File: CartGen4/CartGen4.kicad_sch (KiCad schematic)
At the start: 0 parts

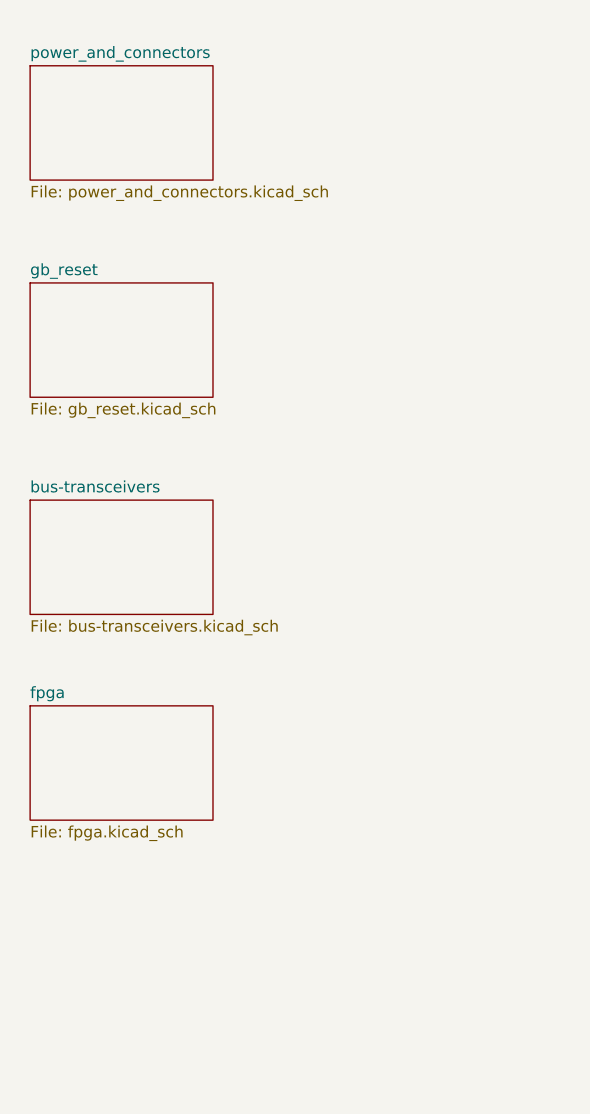
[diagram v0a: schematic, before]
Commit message: Added FPGA and RAM symbols
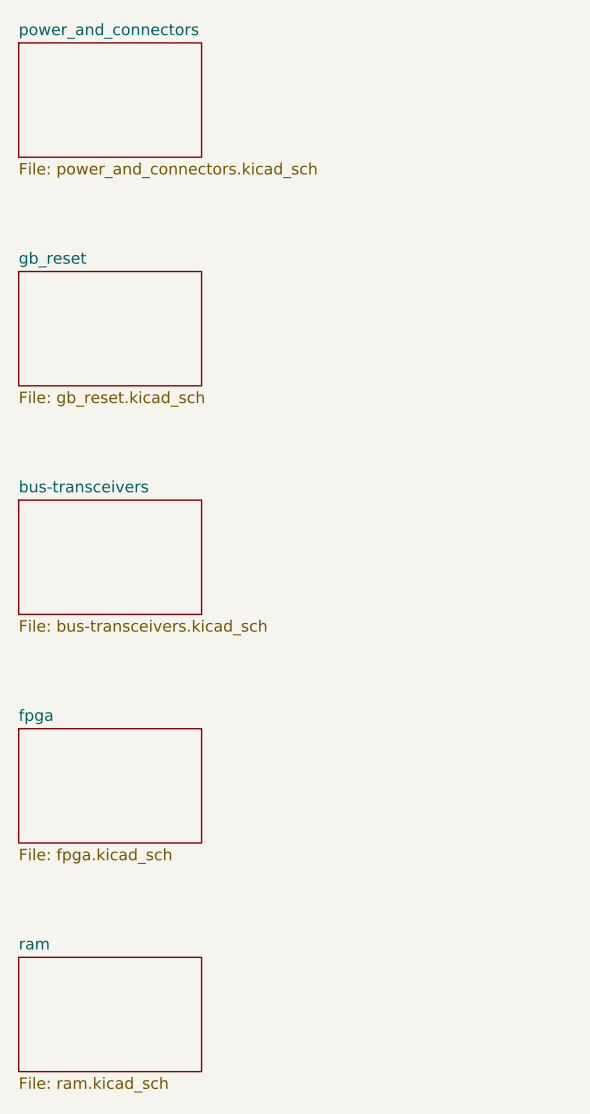
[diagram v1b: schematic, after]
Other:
- added sheet ram (ram.kicad_sch)
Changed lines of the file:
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@@
 (kicad_sch (version 20211123) (generator eeschema)
   (paper "A4")
-  (sheet (at 26.67 40.64) (size 20.32 12.7) (fields_autoplaced)
-    (stroke (width 0.1524) (type solid) (color 0 0 0 0))
-    (fill (color 0 0 0 0.0000))
-    (property "Sheet name" "power_and_connectors" (id 0) (at 26.67 39.9284 0)
-      (effects (font (size 1.27 1.27)) (justify left bottom))
-    )
-    (property "Sheet file" "power_and_connectors.kicad_sch" (id 1) (at 26.67 53.9246 0)
-      (effects (font (size 1.27 1.27)) (justify left top))
-    )
-  )
-  (sheet (at 26.67 88.9) (size 20.32 12.7) (fields_autoplaced)
-    (stroke (width 0.1524) (type solid) (color 0 0 0 0))
-    (fill (color 0 0 0 0.0000))
-    (property "Sheet name" "bus-transceivers" (id 0) (at 26.67 88.1884 0)
-      (effects (font (size 1.27 1.27)) (justify left bottom))
-    )
-    (property "Sheet file" "bus-transceivers.kicad_sch" (id 1) (at 26.67 102.1846 0)
-      (effects (font (size 1.27 1.27)) (justify left top))
-    )
-  )
-  (sheet (at 26.67 64.77) (size 20.32 12.7) (fields_autoplaced)
-    (stroke (width 0.1524) (type solid) (color 0 0 0 0))
-    (fill (color 0 0 0 0.0000))
-    (property "Sheet name" "gb_reset" (id 0) (at 26.67 64.0584 0)
-      (effects (font (size 1.27 1.27)) (justify left bottom))
-    )
-    (property "Sheet file" "gb_reset.kicad_sch" (id 1) (at 26.67 78.0546 0)
-      (effects (font (size 1.27 1.27)) (justify left top))
-    )
-  )
-  (sheet (at 26.67 111.76) (size 20.32 12.7) (fields_autoplaced)
-    (stroke (width 0.1524) (type solid) (color 0 0 0 0))
-    (fill (color 0 0 0 0.0000))
-    (property "Sheet name" "fpga" (id 0) (at 26.67 111.0484 0)
-      (effects (font (size 1.27 1.27)) (justify left bottom))
-    )
-    (property "Sheet file" "fpga.kicad_sch" (id 1) (at 26.67 125.0446 0)
+  (sheet (at 25.4 38.1) (size 20.32 12.7) (fields_autoplaced)
+    (stroke (width 0.1524) (type solid) (color 0 0 0 0))
+    (fill (color 0 0 0 0.0000))
+    (property "Sheet name" "power_and_connectors" (id 0) (at 25.4 37.3884 0)
+      (effects (font (size 1.27 1.27)) (justify left bottom))
+    )
+    (property "Sheet file" "power_and_connectors.kicad_sch" (id 1) (at 25.4 51.3846 0)
+      (effects (font (size 1.27 1.27)) (justify left top))
+    )
+  )
+  (sheet (at 25.4 88.9) (size 20.32 12.7) (fields_autoplaced)
+    (stroke (width 0.1524) (type solid) (color 0 0 0 0))
+    (fill (color 0 0 0 0.0000))
+    (property "Sheet name" "bus-transceivers" (id 0) (at 25.4 88.1884 0)
+      (effects (font (size 1.27 1.27)) (justify left bottom))
+    )
+    (property "Sheet file" "bus-transceivers.kicad_sch" (id 1) (at 25.4 102.1846 0)
+      (effects (font (size 1.27 1.27)) (justify left top))
+    )
+  )
+  (sheet (at 25.4 139.7) (size 20.32 12.7) (fields_autoplaced)
+    (stroke (width 0.1524) (type solid) (color 0 0 0 0))
+    (fill (color 0 0 0 0.0000))
+    (property "Sheet name" "ram" (id 0) (at 25.4 138.9884 0)
+      (effects (font (size 1.27 1.27)) (justify left bottom))
+    )
+    (property "Sheet file" "ram.kicad_sch" (id 1) (at 25.4 152.9846 0)
+      (effects (font (size 1.27 1.27)) (justify left top))
+    )
+  )
+  (sheet (at 25.4 63.5) (size 20.32 12.7) (fields_autoplaced)
+    (stroke (width 0.1524) (type solid) (color 0 0 0 0))
+    (fill (color 0 0 0 0.0000))
+    (property "Sheet name" "gb_reset" (id 0) (at 25.4 62.7884 0)
+      (effects (font (size 1.27 1.27)) (justify left bottom))
+    )
+    (property "Sheet file" "gb_reset.kicad_sch" (id 1) (at 25.4 76.7846 0)
+      (effects (font (size 1.27 1.27)) (justify left top))
+    )
+  )
+  (sheet (at 25.4 114.3) (size 20.32 12.7) (fields_autoplaced)
+    (stroke (width 0.1524) (type solid) (color 0 0 0 0))
+    (fill (color 0 0 0 0.0000))
+    (property "Sheet name" "fpga" (id 0) (at 25.4 113.5884 0)
+      (effects (font (size 1.27 1.27)) (justify left bottom))
+    )
+    (property "Sheet file" "fpga.kicad_sch" (id 1) (at 25.4 127.5846 0)
       (effects (font (size 1.27 1.27)) (justify left top))
     )
@@
     (path "/67020394-371c-451d-9641-dd6c212cfc5e" (page "4"))
     (path "/89c162de-8374-4cb6-9c74-abac2a052a8d" (page "5"))
+    (path "/6fc5aafb-5a22-4bda-8f08-f38eb0e112cc" (page "6"))
   )
   (symbol_instances
@@
       (reference "C25") (unit 1) (value "0.022uF") (footprint "")
     )
-    (path "/89c162de-8374-4cb6-9c74-abac2a052a8d/779a694e-7da6-4a21-b5eb-83d9a87bedcf"
-      (reference "IC?") (unit 1) (value "LFXP2-8E-5MN132C") (footprint "BGA132C50P14X14_800X800X135")
-    )
     (path "/4ef07d45-f940-4cb6-bb96-2ddec13fd099/42ea6df8-6ad7-4a48-a860-9865d99a1cf3"
       (reference "L1") (unit 1) (value "10u") (footprint "Inductor_SMD:L_1008_2520Metric")
@@
       (reference "U4") (unit 1) (value "SN74AVC16827DGGR") (footprint "")
     )
-  )
+    (path "/89c162de-8374-4cb6-9c74-abac2a052a8d/3b80cf20-b12b-49a6-84bd-473603c85348"
+      (reference "U?") (unit 1) (value "LFXP2-8E-5MN132C") (footprint "")
+    )
+    (path "/6fc5aafb-5a22-4bda-8f08-f38eb0e112cc/583b625d-197e-4c6f-9f56-0c49ec079aa7"
+      (reference "U?") (unit 1) (value "AS1C8M16PL-70BIN") (footprint "BGA49C50P7X7_400X400X100")
+    )
+    (path "/89c162de-8374-4cb6-9c74-abac2a052a8d/1765047d-477d-4e9e-a14b-c311772de8ac"
+      (reference "U?") (unit 2) (value "LFXP2-8E-5MN132C") (footprint "")
+    )
+    (path "/89c162de-8374-4cb6-9c74-abac2a052a8d/f61655d7-5449-47b8-9e48-9d7ea80abb6f"
+      (reference "U?") (unit 3) (value "LFXP2-8E-5MN132C") (footprint "")
+    )
+    (path "/89c162de-8374-4cb6-9c74-abac2a052a8d/c39ad1a9-2c59-481d-9cf3-32a127a43b1d"
+      (reference "U?") (unit 4) (value "LFXP2-8E-5MN132C") (footprint "")
+    )
+    (path "/89c162de-8374-4cb6-9c74-abac2a052a8d/03031b1d-3503-4fbb-bb1d-d0daee267daa"
+      (reference "U?") (unit 5) (value "LFXP2-8E-5MN132C") (footprint "")
+    )
+    (path "/89c162de-8374-4cb6-9c74-abac2a052a8d/c0ae4ece-7462-465e-9c01-02b01c36e260"
+      (reference "U?") (unit 6) (value "LFXP2-8E-5MN132C") (footprint "")
+    )
+    (path "/89c162de-8374-4cb6-9c74-abac2a052a8d/f190f8af-9d18-4cca-84ff-7cbb88c4fd8f"
+      (reference "U?") (unit 7) (value "LFXP2-8E-5MN132C") (footprint "")
+    )
+    (path "/89c162de-8374-4cb6-9c74-abac2a052a8d/348f0dc1-2fce-4d8e-8a95-66b79092ec52"
+      (reference "U?") (unit 8) (value "LFXP2-8E-5MN132C") (footprint "")
+    )
+    (path "/89c162de-8374-4cb6-9c74-abac2a052a8d/b7d43457-8a30-461a-9b4f-a37a3e412df8"
+      (reference "U?") (unit 9) (value "LFXP2-8E-5MN132C") (footprint "")
+    )
+    (path "/89c162de-8374-4cb6-9c74-abac2a052a8d/2c70d510-d60c-4bed-aef6-47a1a52339b8"
+      (reference "U?") (unit 10) (value "LFXP2-8E-5MN132C") (footprint "")
+    )
+  )

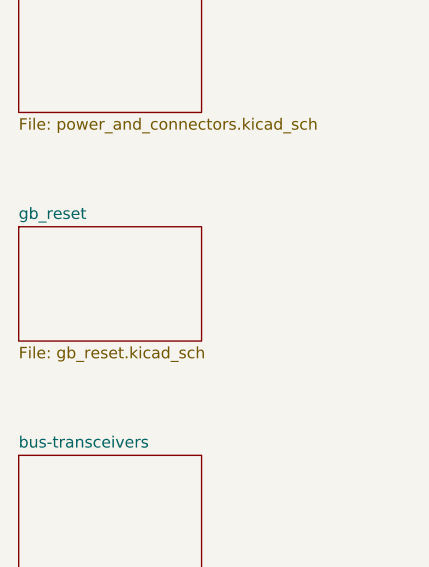
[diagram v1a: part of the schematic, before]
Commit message: Added RAM and clock
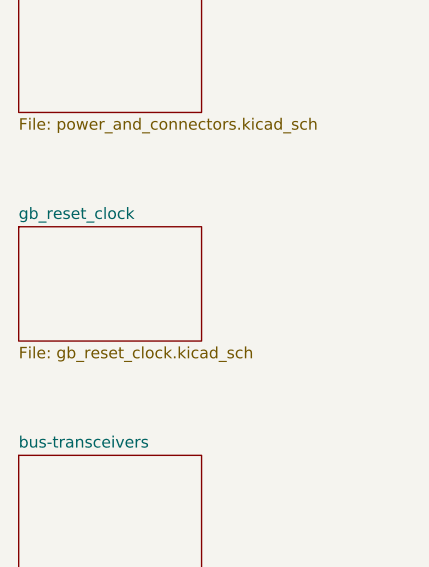
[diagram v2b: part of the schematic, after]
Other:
- sheet gb_reset renamed gb_reset_clock
- sheet gb_reset_clock: file gb_reset.kicad_sch -> gb_reset_clock.kicad_sch
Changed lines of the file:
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@@
     (stroke (width 0.1524) (type solid) (color 0 0 0 0))
     (fill (color 0 0 0 0.0000))
-    (property "Sheet name" "gb_reset" (id 0) (at 25.4 62.7884 0)
+    (property "Sheet name" "gb_reset_clock" (id 0) (at 25.4 62.7884 0)
       (effects (font (size 1.27 1.27)) (justify left bottom))
     )
-    (property "Sheet file" "gb_reset.kicad_sch" (id 1) (at 25.4 76.7846 0)
+    (property "Sheet file" "gb_reset_clock.kicad_sch" (id 1) (at 25.4 76.7846 0)
       (effects (font (size 1.27 1.27)) (justify left top))
     )
@@
       (reference "#PWR043") (unit 1) (value "+3V3") (footprint "")
     )
+    (path "/6fc5aafb-5a22-4bda-8f08-f38eb0e112cc/3fd33b03-7670-43ea-b3a6-f7ebadfe90c5"
+      (reference "#PWR044") (unit 1) (value "+1V8") (footprint "")
+    )
+    (path "/6fc5aafb-5a22-4bda-8f08-f38eb0e112cc/c9b93426-ce76-45db-8747-0eb2d84f311f"
+      (reference "#PWR045") (unit 1) (value "GND") (footprint "")
+    )
+    (path "/6fc5aafb-5a22-4bda-8f08-f38eb0e112cc/3bfbb624-7bc3-48cd-9598-b9cd115b2755"
+      (reference "#PWR046") (unit 1) (value "GND") (footprint "")
+    )
+    (path "/6fc5aafb-5a22-4bda-8f08-f38eb0e112cc/9bc03fc6-f8b5-445b-8d8e-61d63f390d19"
+      (reference "#PWR047") (unit 1) (value "+1V8") (footprint "")
+    )
+    (path "/6fc5aafb-5a22-4bda-8f08-f38eb0e112cc/8f3d8788-ba9d-4e57-bddb-748ec78e349a"
+      (reference "#PWR048") (unit 1) (value "+1V8") (footprint "")
+    )
+    (path "/6fc5aafb-5a22-4bda-8f08-f38eb0e112cc/779ea120-14c2-46ca-84bd-530b5b31ae64"
+      (reference "#PWR049") (unit 1) (value "GND") (footprint "")
+    )
+    (path "/76bc839d-93e8-4c60-b95d-ac552335ae99/06c4b97a-5686-4633-a89a-22345d72cbad"
+      (reference "#PWR?") (unit 1) (value "+1V8") (footprint "")
+    )
+    (path "/76bc839d-93e8-4c60-b95d-ac552335ae99/339d5868-10a9-4e52-aa60-655935cc0b87"
+      (reference "#PWR?") (unit 1) (value "+1V8") (footprint "")
+    )
+    (path "/76bc839d-93e8-4c60-b95d-ac552335ae99/4c3e2699-7deb-4821-b0d7-fe031018757f"
+      (reference "#PWR?") (unit 1) (value "+1V8") (footprint "")
+    )
+    (path "/76bc839d-93e8-4c60-b95d-ac552335ae99/96d12c28-3355-42ed-9ed2-74043f645886"
+      (reference "#PWR?") (unit 1) (value "GND") (footprint "")
+    )
+    (path "/76bc839d-93e8-4c60-b95d-ac552335ae99/b9d3bb68-0fb3-47f8-9194-6a6ffdf2366d"
+      (reference "#PWR?") (unit 1) (value "+1V8") (footprint "")
+    )
+    (path "/76bc839d-93e8-4c60-b95d-ac552335ae99/f06f7a16-2d12-4c79-b494-519499033b3d"
+      (reference "#PWR?") (unit 1) (value "GND") (footprint "")
+    )
     (path "/4ef07d45-f940-4cb6-bb96-2ddec13fd099/1b8d5810-67b5-41f5-a4e9-e6c2cc9fec50"
       (reference "A1") (unit 1) (value "GBC_Cart") (footprint "Boards:GBC_Cart")
@@
       (reference "C25") (unit 1) (value "0.022uF") (footprint "")
     )
+    (path "/6fc5aafb-5a22-4bda-8f08-f38eb0e112cc/099426c5-dae5-4069-bf55-fdf3f2477fb1"
+      (reference "C26") (unit 1) (value "100n") (footprint "")
+    )
+    (path "/6fc5aafb-5a22-4bda-8f08-f38eb0e112cc/862f650a-bf93-4b86-a4a6-c9ae9d322f23"
+      (reference "C27") (unit 1) (value "100n") (footprint "")
+    )
+    (path "/6fc5aafb-5a22-4bda-8f08-f38eb0e112cc/d2460763-39eb-4ae3-a21d-27585e4fd387"
+      (reference "C28") (unit 1) (value "100n") (footprint "")
+    )
+    (path "/6fc5aafb-5a22-4bda-8f08-f38eb0e112cc/7631e4a2-2c89-4f43-b991-30d0ca1f5129"
+      (reference "C29") (unit 1) (value "100n") (footprint "")
+    )
     (path "/4ef07d45-f940-4cb6-bb96-2ddec13fd099/42ea6df8-6ad7-4a48-a860-9865d99a1cf3"
       (reference "L1") (unit 1) (value "10u") (footprint "Inductor_SMD:L_1008_2520Metric")
@@
       (reference "R?") (unit 1) (value "50K") (footprint "")
     )
+    (path "/76bc839d-93e8-4c60-b95d-ac552335ae99/8456adf8-c894-4d12-81a1-d621382accef"
+      (reference "R?") (unit 1) (value "10K") (footprint "")
+    )
+    (path "/76bc839d-93e8-4c60-b95d-ac552335ae99/c67d28e9-03e2-44f5-bdd8-cfe20cc1581f"
+      (reference "R?") (unit 1) (value "10K") (footprint "")
+    )
     (path "/4ef07d45-f940-4cb6-bb96-2ddec13fd099/e190d083-d82d-481a-a7b8-1c8c0afec670"
       (reference "U1") (unit 1) (value "TPS65266-1RHBR") (footprint "QFN50P500X500X100-33N-D")
@@
       (reference "U4") (unit 1) (value "SN74AVC16827DGGR") (footprint "")
     )
+    (path "/6fc5aafb-5a22-4bda-8f08-f38eb0e112cc/583b625d-197e-4c6f-9f56-0c49ec079aa7"
+      (reference "U5") (unit 1) (value "AS1C8M16PL-70BIN") (footprint "BGA49C50P7X7_400X400X100")
+    )
     (path "/89c162de-8374-4cb6-9c74-abac2a052a8d/3b80cf20-b12b-49a6-84bd-473603c85348"
       (reference "U?") (unit 1) (value "LFXP2-8E-5MN132C") (footprint "")
     )
-    (path "/6fc5aafb-5a22-4bda-8f08-f38eb0e112cc/583b625d-197e-4c6f-9f56-0c49ec079aa7"
-      (reference "U?") (unit 1) (value "AS1C8M16PL-70BIN") (footprint "BGA49C50P7X7_400X400X100")
+    (path "/76bc839d-93e8-4c60-b95d-ac552335ae99/edee174b-c83c-4ee1-ad60-766f4a3fc371"
+      (reference "U?") (unit 1) (value "5X1503L-000NLGI") (footprint "SON40P200X200X110-11N")
     )
     (path "/89c162de-8374-4cb6-9c74-abac2a052a8d/1765047d-477d-4e9e-a14b-c311772de8ac"
